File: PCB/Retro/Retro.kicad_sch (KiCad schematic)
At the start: 24 parts, among them J1 KeyBoard 5,Rd,Ld,D7..0,Gnd, J2 PortB, J3 PortA, J4 COM: Gnd,Rx,Tx,Rts,Dcd,Cts,5v, SW1 SW_Push, U1 74LS92, U10 GAL20V8B-10, U11 GAL20V8B-10, U2 R65C02, U3 CD4059A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

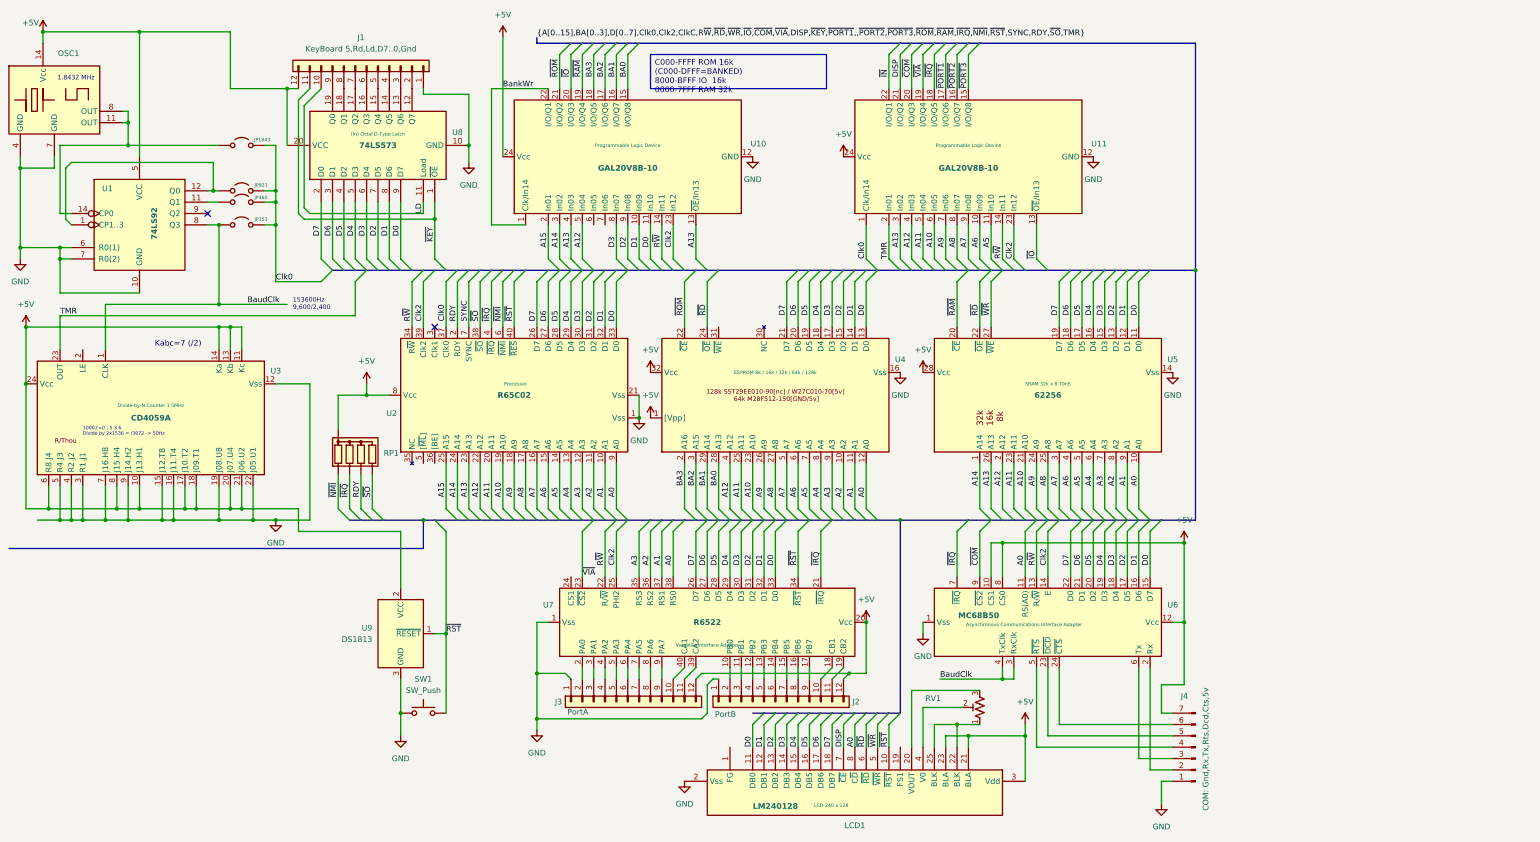
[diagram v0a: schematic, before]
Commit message: Added RST switch and address connector
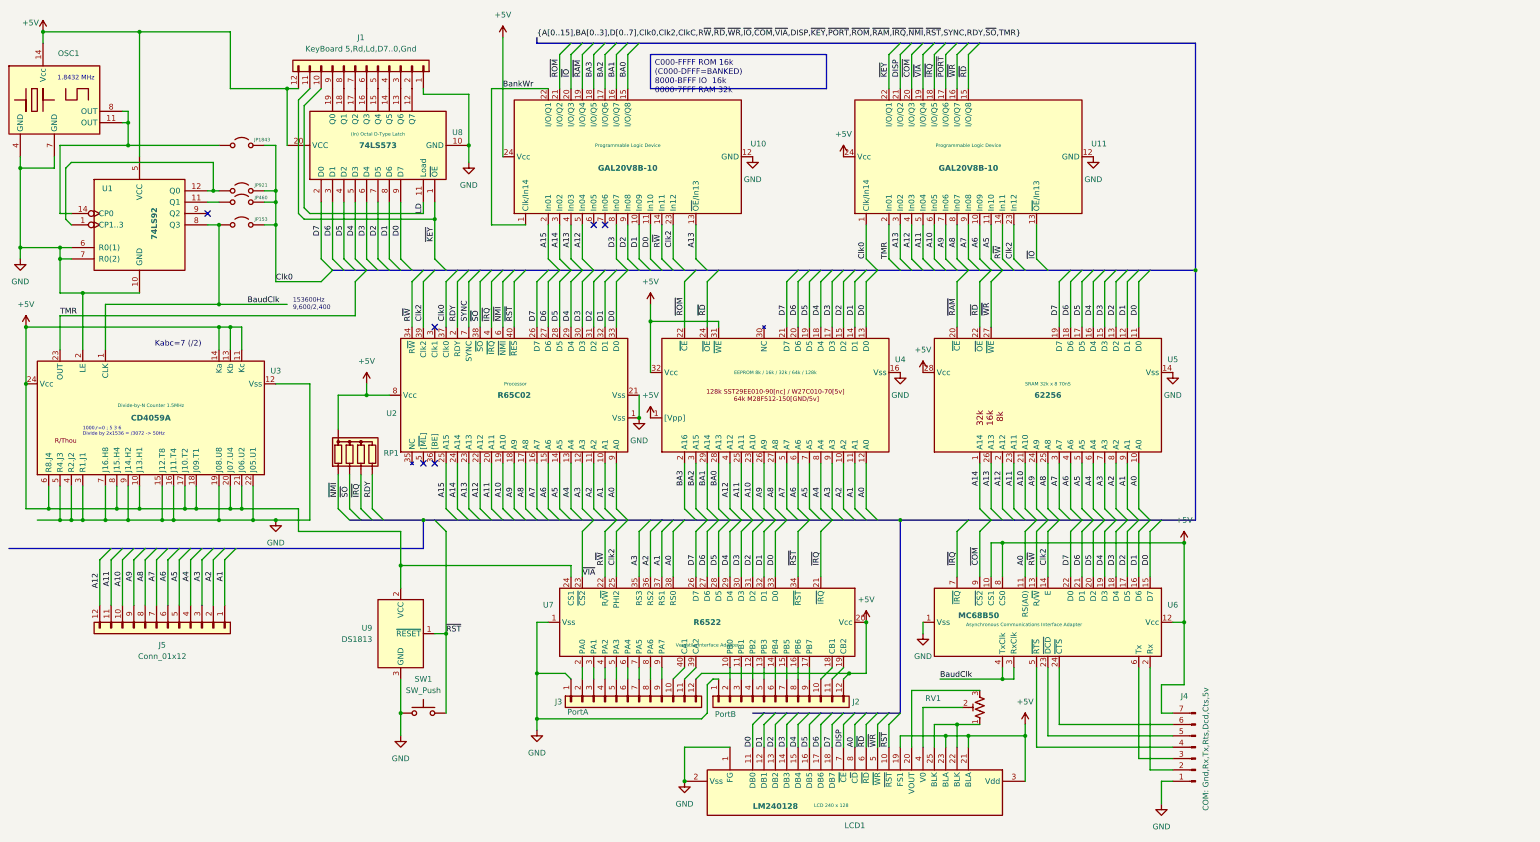
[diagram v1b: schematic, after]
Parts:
- added J5: Conn_01x12, Connector_PinSocket_2.54mm:PinSocket_1x12_P2.54mm_Vertical, symbol RetroParts_Library:Conn_01x12
- SW1: footprint Button_Switch_THT:KSA_Tactile_SPST -> Library:MiniSwitch
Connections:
- net ~{IN} is gone; now on net ~{KEY}: U11.22 (I/O/Q1)
- net ~{PORT2} is gone; now on net ~{WR}: U11.16 (I/O/Q7)
- net ~{PORT3} is gone; now on net ~{RD}: U11.15 (I/O/Q8)
- net +5V: now also LCD1.19 (FS1), U4.31 (~{WE}), U7.24 (CS1)
- net A1: now also J5.1 (Pin_1)
- net A10: now also J5.10 (Pin_10)
- net A11: now also J5.11 (Pin_11)
- net A12: now also J5.12 (Pin_12)
- net A2: now also J5.2 (Pin_2)
- net A3: now also J5.3 (Pin_3)
- net A4: now also J5.4 (Pin_4)
- net A5: now also J5.5 (Pin_5)
- net A6: now also J5.6 (Pin_6)
- net A7: now also J5.7 (Pin_7)
- net A8: now also J5.8 (Pin_8)
- net A9: now also J5.9 (Pin_9)
- net GND: now also LCD1.1 (FG), U3.2 (LE)
- net RDY: now also RP1.5 (R4); no longer RP1.4 (R3)
- net ~{IRQ}: now also RP1.4 (R3); no longer RP1.3 (R2)
- net ~{SO}: now also RP1.3 (R2); no longer RP1.5 (R4)
- net ~{PORT1} renamed ~{PORT}
- no-connect marks 2 -> 6
